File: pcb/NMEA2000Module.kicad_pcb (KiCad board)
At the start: 2 copper layers, 78 x 124 mm, 40 parts, among them IC1 MCP2562FD, K1 1W1, P1 PULSE_IN, P3 TERM_R, P4 CAN, P7 I2C1, P9 ANALOG IN, U1 74HC14, U2 ESP32Dev, U3 JDY40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

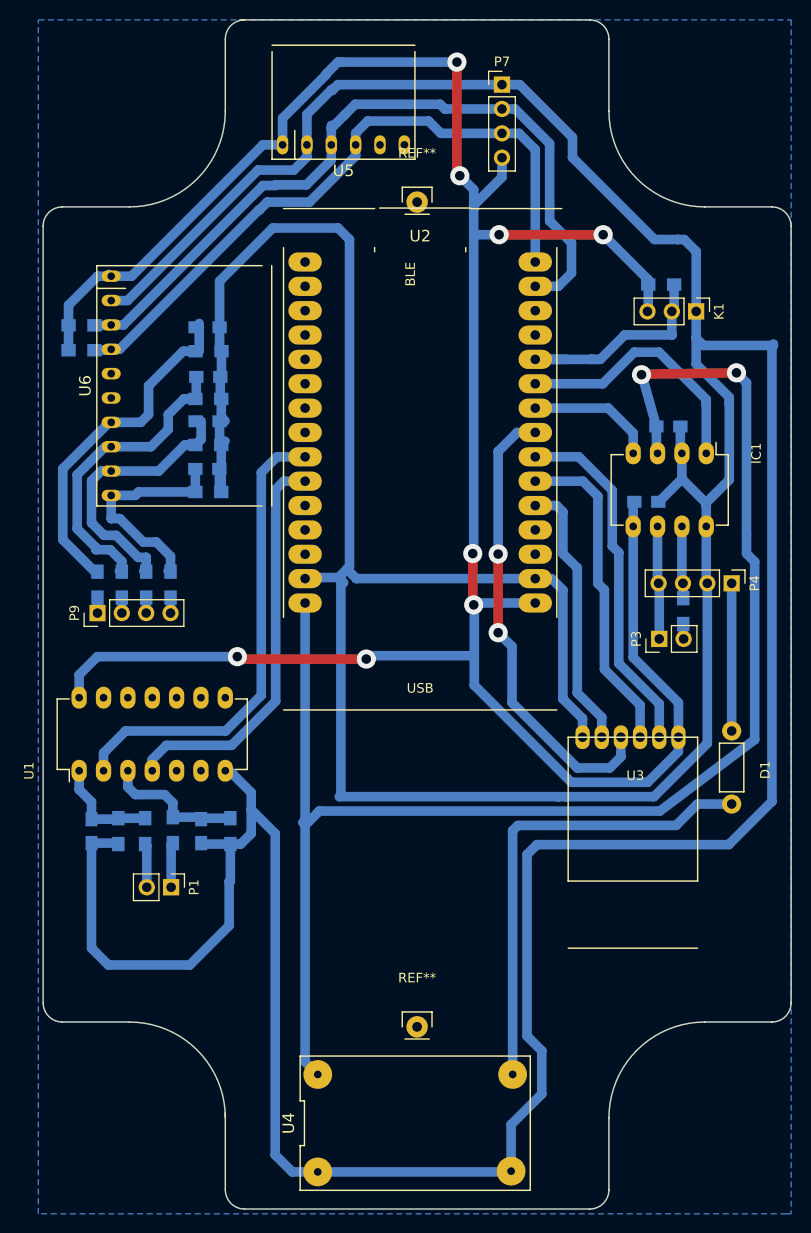
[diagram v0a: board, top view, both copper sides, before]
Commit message: Added RF code not tested, and high voltage protection diodes
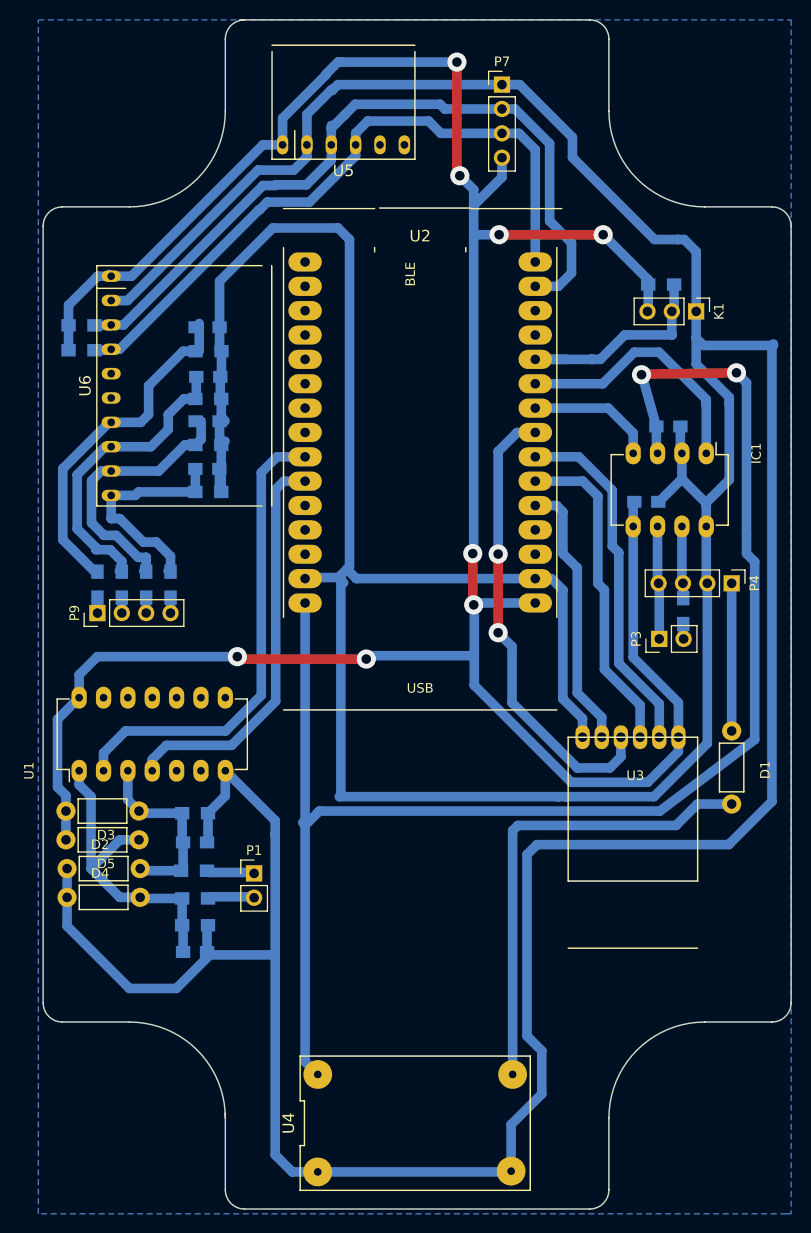
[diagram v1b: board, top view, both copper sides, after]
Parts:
- removed REF** (x2): Pin_Header_Straight_1x01, Pin_Headers:Pin_Header_Straight_1x01
- added D2: DIODE, Resistors_ThroughHole:Resistor_Horizontal_RM7mm, F.Cu at (108.5, 138.0)
- added D3: DIODE, Resistors_ThroughHole:Resistor_Horizontal_RM7mm, F.Cu at (101.0, 144.0)
- added D4: DIODE, Resistors_ThroughHole:Resistor_Horizontal_RM7mm, F.Cu at (108.5, 141.0)
- added D5: DIODE, Resistors_ThroughHole:Resistor_Horizontal_RM7mm, F.Cu at (101.0, 147.0)
- moved C4 16.6 mm to (114.3, 152.7), turned to 0 degrees
- moved R4 12.7 mm to (114.3, 149.9), turned to 180 degrees
- moved P1 8.77 mm to (120.5, 144.5), turned to 0 degrees
- moved R3 8.74 mm to (114.3, 147.1), turned to 180 degrees
- moved R1 4.78 mm to (114.2, 144.2), turned to 180 degrees
- moved R2 4.13 mm to (114.3, 138.2), turned to 0 degrees
- moved C2 1.34 mm to (114.3, 141.3), turned to 0 degrees
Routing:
- net Net-(C4-Pad1): track 11.2 -> 33.4 mm
- net 3v3: track 260.0 -> 276.2 mm
- net Net-(C2-Pad1): track 14.6 -> 19.9 mm
- net GND: track 568.5 -> 565.2 mm

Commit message: Added BMP280 sensor and changed to LDO regulator
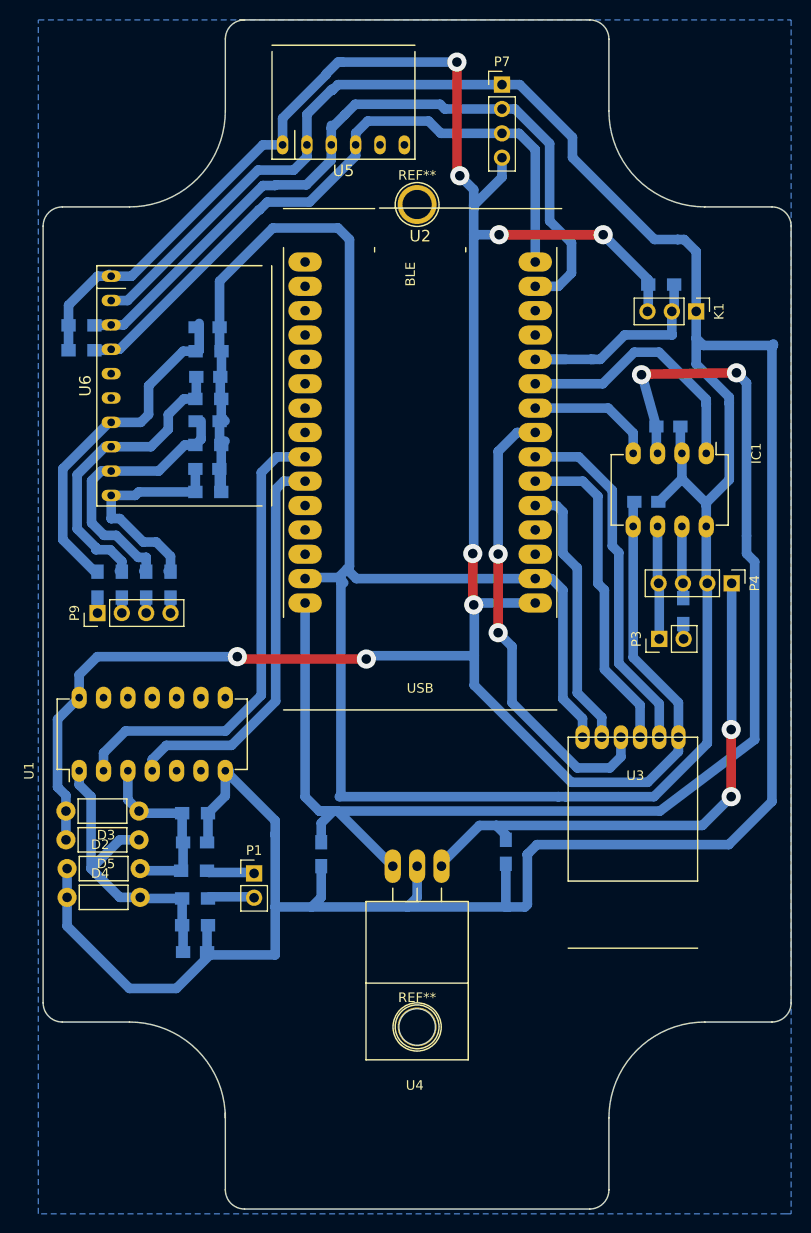
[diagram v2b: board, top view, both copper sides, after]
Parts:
- removed D1: DIODE, Resistors_ThroughHole:Resistor_Horizontal_RM7mm
- added C10: 100nF, Capacitors_SMD:C_0805_HandSoldering, B.Cu at (127.5, 142.5)
- added C9: 330nF, Capacitors_SMD:C_0805_HandSoldering, B.Cu at (146.8, 142.2)
- added REF**: 1pin, Connect:1pin, F.Cu at (137.5, 74.8)
- added REF**: 1pin, Connect:1pin, F.Cu at (137.5, 160.5)
- U4: value DCDCConverter -> LM7805CT; footprint Divers:DC-DC-Converter -> TO_SOT_Packages_THT:TO-220_Neutral123_Horizontal_LargePads
- moved U4 26.8 mm to (137.5, 143.8), turned to 180 degrees
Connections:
- U4 pad 1: Net-(D1-Pad2) -> 12v
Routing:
- net Net-(D1-Pad2): track 49.9 -> 0.00 mm
- net 12v: track 15.4 -> 57.6 mm, vias 0 -> 2
- net GND: track 565.2 -> 529.9 mm
- net 5v: track 157.7 -> 141.5 mm

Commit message: Added BT switch and engine on support
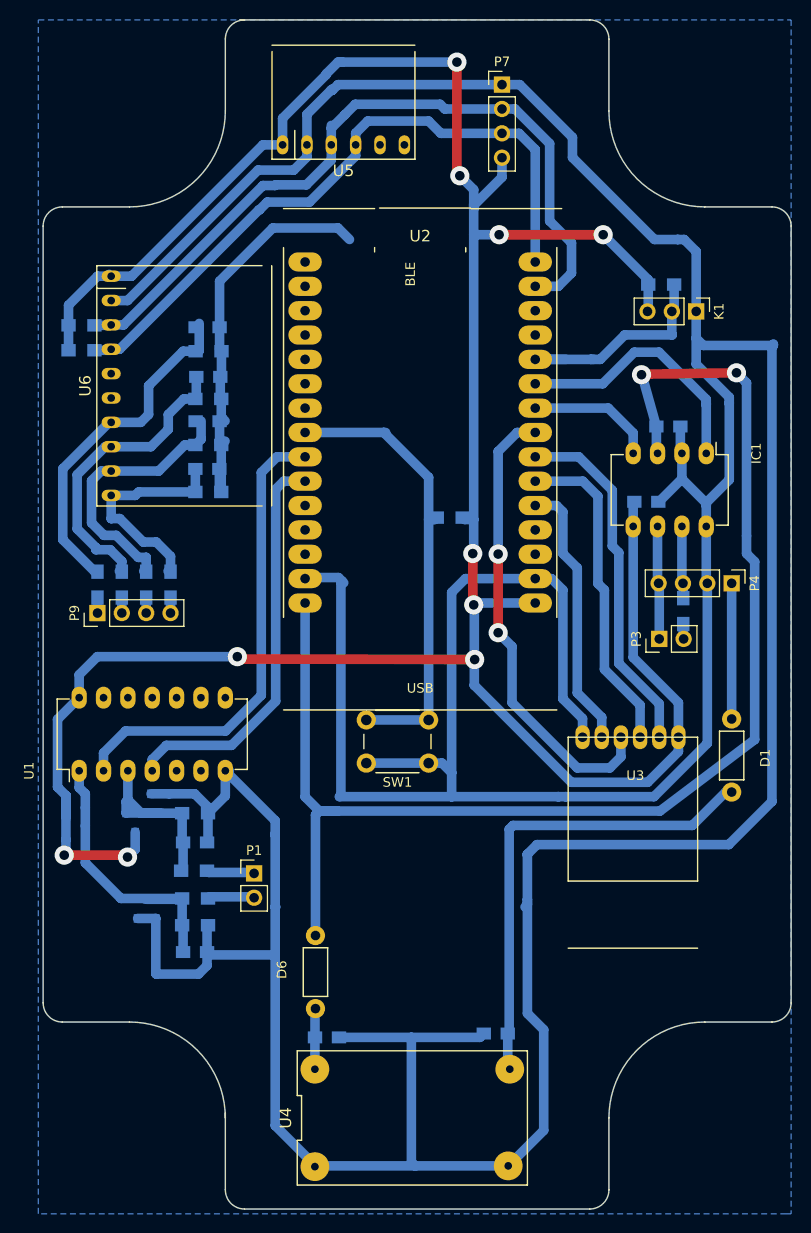
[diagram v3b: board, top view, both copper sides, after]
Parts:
- removed REF** (x2): 1pin, Connect:1pin
- added D1: DIODESCH, Resistors_ThroughHole:Resistor_Horizontal_RM7mm, F.Cu at (170.3, 128.4)
- added D6: DIODESCH, Resistors_ThroughHole:Resistor_Horizontal_RM7mm, F.Cu at (126.9, 158.6)
- added R5: 10K, Resistors_SMD:R_0805_HandSoldering, B.Cu at (140.9, 107.4)
- added SW1: BT Enable, Buttons_Switches_ThroughHole:SW_PUSH_6mm, F.Cu at (138.7, 133.0)
- D2, D3, D4, D5: footprint Resistors_ThroughHole:Resistor_Horizontal_RM7mm -> TO_SOT_Packages_SMD:SOT-23; moved to B.Cu
- U4: value LM7805CT -> DCDCConverter; footprint TO_SOT_Packages_THT:TO-220_Neutral123_Horizontal_LargePads -> Divers:DC-DC-Converter
- moved U4 26.3 mm to (137.0, 170.0), turned to 0 degrees
- moved C10 19.1 mm to (128.1, 161.6), turned to 0 degrees
- moved C9 19.0 mm to (145.7, 161.2), turned to 180 degrees
- moved D3 11.8 mm to (110.7, 137.2), turned to 270 degrees
- moved D5 8.39 mm to (109.3, 148.2), turned to 90 degrees
- moved D4 7.02 mm to (101.9, 138.6)
- moved D2 1.26 mm to (108.1, 139.2), turned to 270 degrees
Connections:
- C10 pad 1: 5v -> Net-(C10-Pad1)
- C9 pad 1: 12v -> Net-(C9-Pad1)
- U2 pad 8: (no net) -> BTENABLE
- U4 pad 1: 12v -> Net-(C9-Pad1)
- U4 pad 3: 5v -> Net-(C10-Pad1)
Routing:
- net Net-(C9-Pad1): track 0.00 -> 50.0 mm
- net BTENABLE: track 0.00 -> 47.8 mm
- net GND: track 529.9 -> 574.3 mm
- net 12v: track 57.6 -> 14.2 mm, vias 2 -> 0
- net 3v3: track 276.2 -> 291.3 mm, vias 8 -> 10
- net Net-(C10-Pad1): track 0.00 -> 6.34 mm
- net Net-(C4-Pad1): track 33.4 -> 30.9 mm
- net 5v: track 141.5 -> 142.7 mm
- net Net-(C2-Pad1): track 19.9 -> 20.5 mm

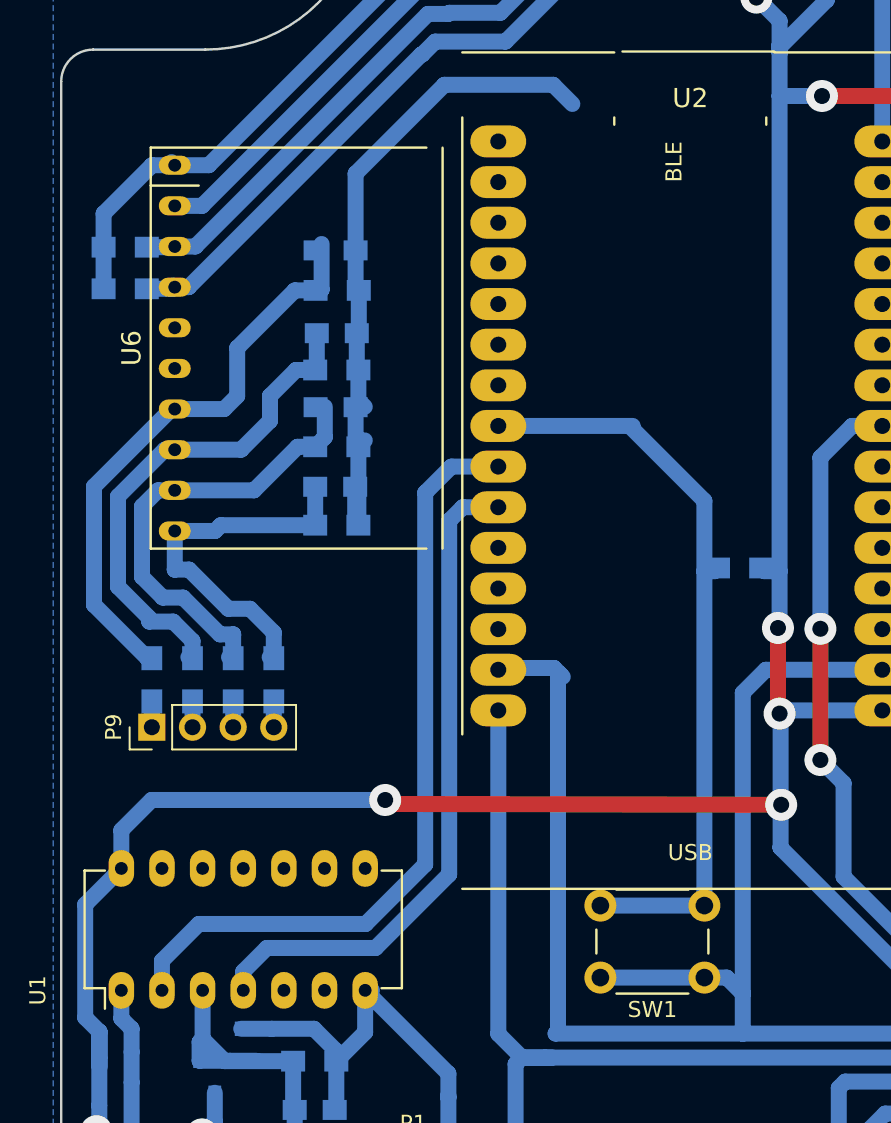
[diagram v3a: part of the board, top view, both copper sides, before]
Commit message: Added better support for simulation and alarms
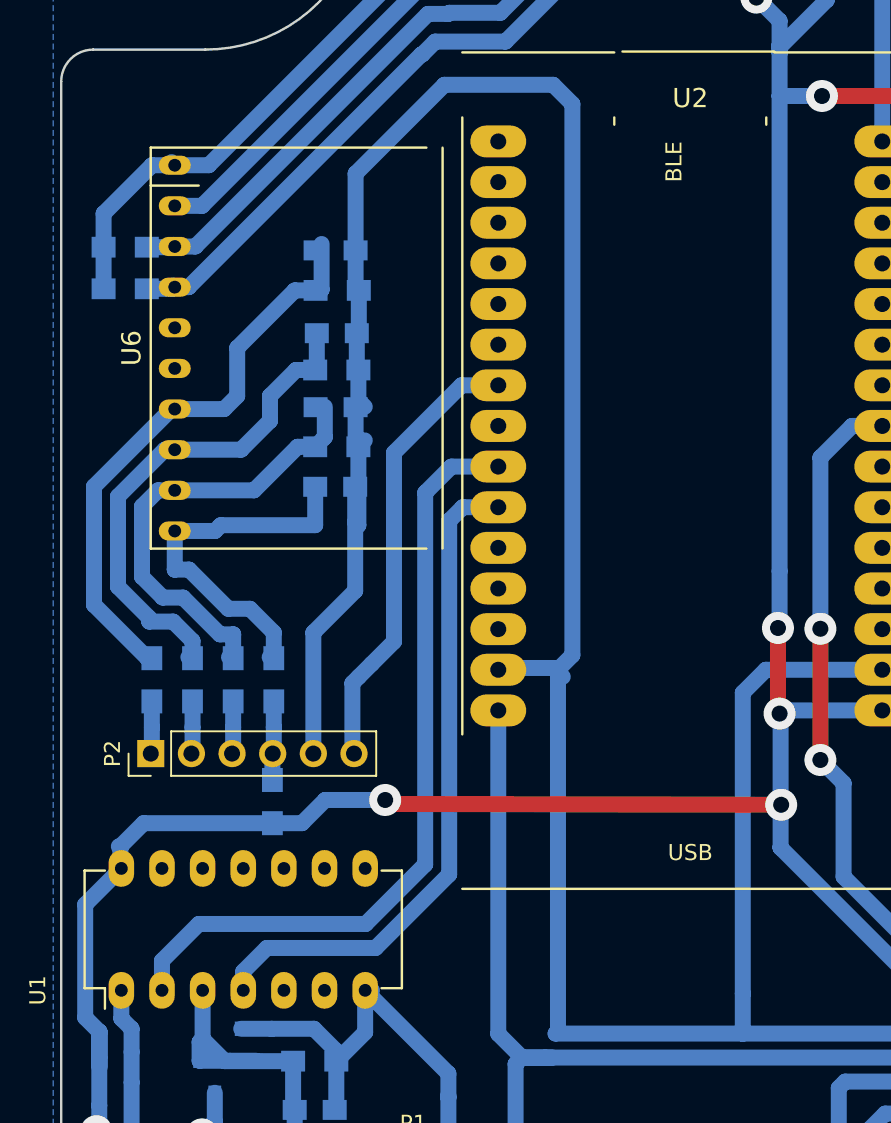
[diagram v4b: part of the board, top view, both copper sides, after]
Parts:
- removed P9: ANALOG IN, Pin_Headers:Pin_Header_Straight_1x04_Pitch2.54mm
- removed R5: 10K, Resistors_SMD:R_0805_HandSoldering
- removed SW1: BT Enable, Buttons_Switches_ThroughHole:SW_PUSH_6mm
- added P2: CONN_6, Pin_Headers:Pin_Header_Straight_1x06_Pitch2.54mm, F.Cu at (104.1, 119.0)
- moved R14 17.7 mm to (111.7, 122.0), turned to 90 degrees
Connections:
- R13 pad 1: Net-(P9-Pad4) -> Net-(P2-Pad4)
- R14 pad 1: Net-(C8-Pad1) -> 3v3
- R14 pad 2: GND -> Net-(P2-Pad4)
- U2 pad 7: (no net) -> BTENABLE
- U2 pad 8: BTENABLE -> (no net)
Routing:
- net GND: track 574.3 -> 616.4 mm
- net BTENABLE: track 47.8 -> 28.2 mm
- net Net-(P2-Pad4): track 0.00 -> 4.95 mm
- net Net-(P2-Pad1): track 1.61 -> 3.29 mm
- net Net-(P2-Pad3): track 1.61 -> 3.29 mm
- net Net-(P2-Pad2): track 1.61 -> 3.29 mm
- net 3v3: track 291.3 -> 289.7 mm
- net Net-(P9-Pad4): track 1.61 -> 0.00 mm
